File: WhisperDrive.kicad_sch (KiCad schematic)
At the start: 9 parts, among them J1 Fan+, J2 Fan+, J3 MOSFET-, J4 Fan-

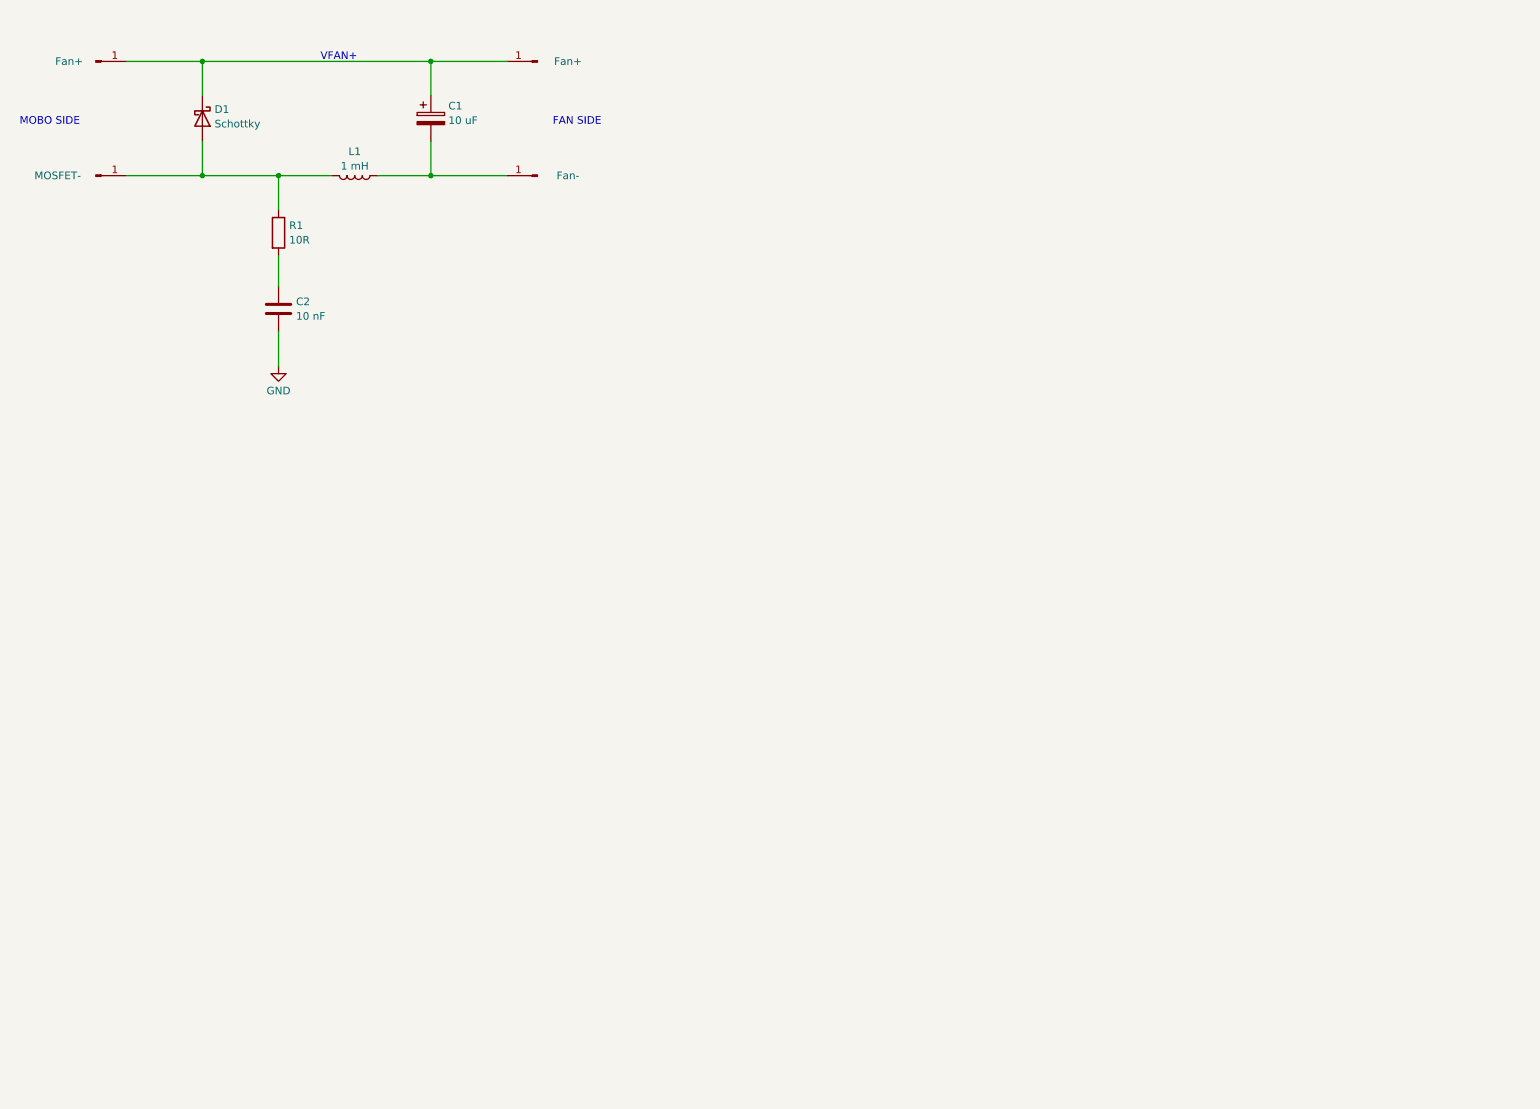
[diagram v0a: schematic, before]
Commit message: Further component selection and preliminary one-block layout for the switching only. Need buffer. Removed second block.
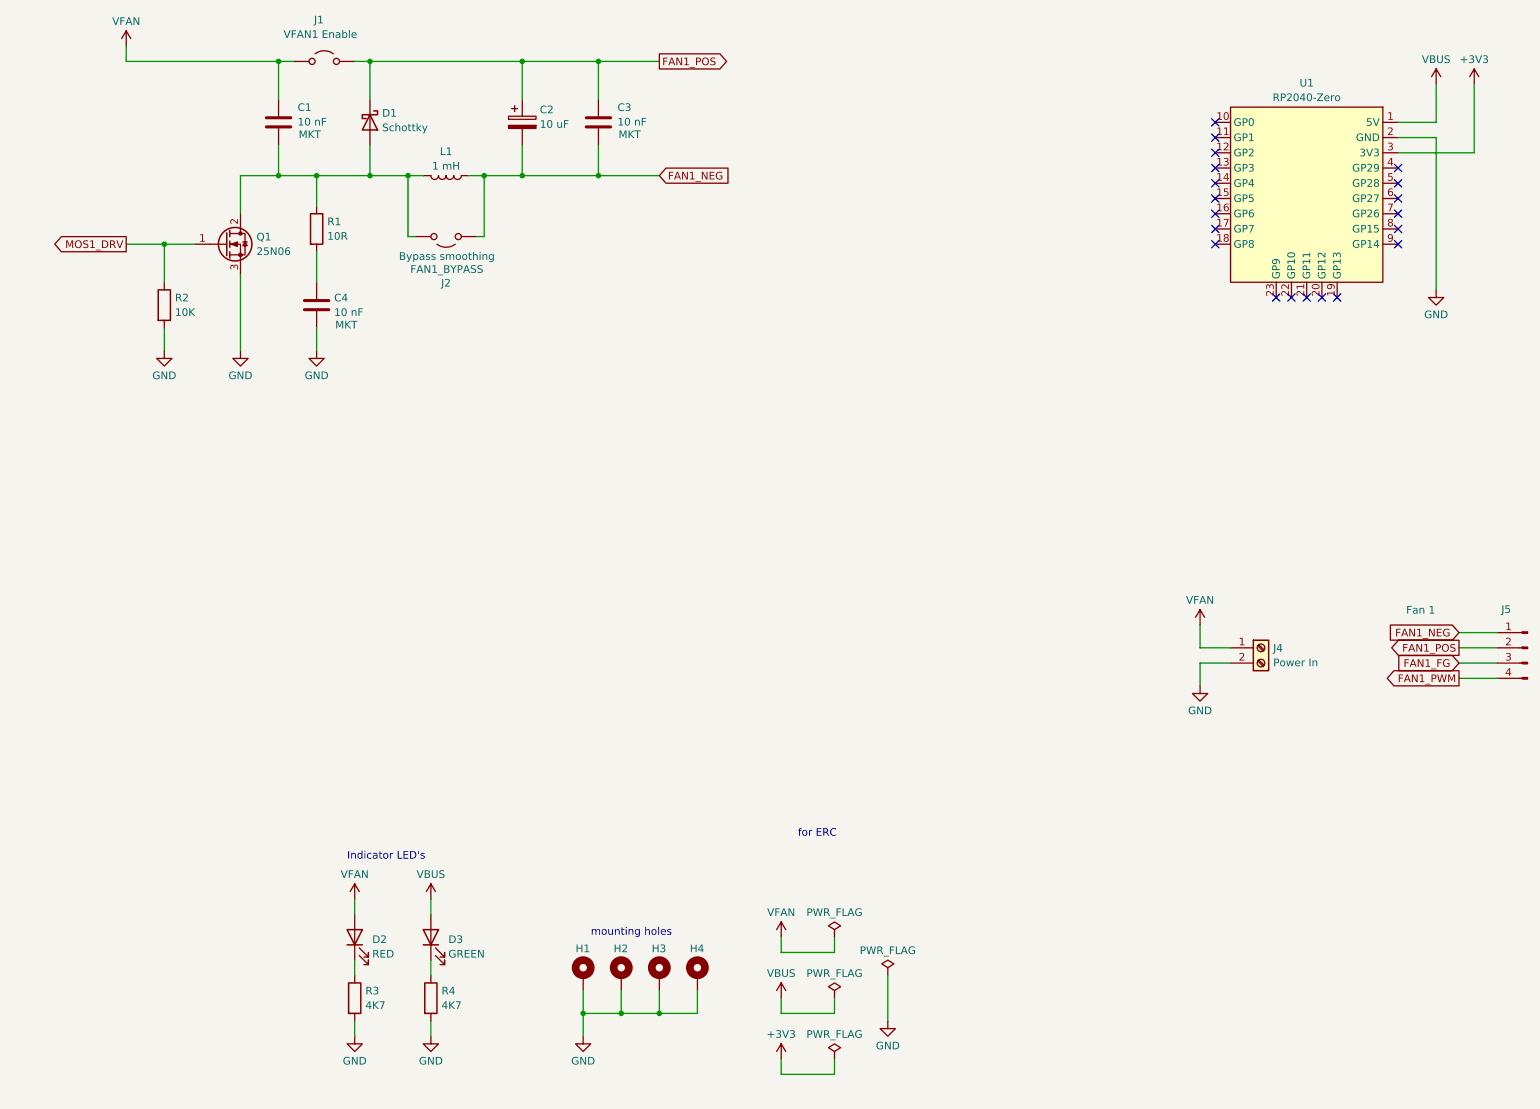
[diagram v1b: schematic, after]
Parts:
- removed J1, J2: Fan+, symbol Connector:Conn_01x01_Pin
- removed J3: MOSFET-, symbol Connector:Conn_01x01_Pin
- removed J4: Fan-, symbol Connector:Conn_01x01_Pin
- added C1, C3: 10 nF, Capacitor_THT:C_Disc_D6.0mm_W2.5mm_P5.00mm, symbol Device:C
- added D2: RED, LED_THT:LED_D3.0mm_Clear, symbol Device:LED
- added D3: GREEN, LED_THT:LED_D3.0mm_Clear, symbol Device:LED
- added H1, H2, H3, H4: MountingHole_Pad, MountingHole:MountingHole_3.2mm_M3, symbol Mechanical:MountingHole_Pad
- added J1: VFAN1 Enable, Jumper:SolderJumper-2_P1.3mm_Bridged2Bar_Pad1.0x1.5mm, symbol Jumper:Jumper_2_Open
- added J2: FAN1_BYPASS, Jumper:SolderJumper-2_P1.3mm_Open_Pad1.0x1.5mm, symbol Jumper:Jumper_2_Open
- added J4: Power In, symbol Connector:Screw_Terminal_01x02
- added J5: Fan 1, Connector_Molex:Molex_KK-254_AE-6410-04A_1x04_P2.54mm_Vertical, symbol Connector:Conn_01x04_Pin
- added Q1: 25N06, Package_TO_SOT_SMD:TO-252-3_TabPin2, symbol Transistor_FET:Q_NMOS_GDS
- added R2: 10K, Resistor_THT:R_Axial_DIN0204_L3.6mm_D1.6mm_P7.62mm_Horizontal, symbol Device:R
- added R3, R4: 4K7, Resistor_THT:R_Axial_DIN0204_L3.6mm_D1.6mm_P7.62mm_Horizontal, symbol Device:R
- added U1: RP2040-Zero, RP2040-Zero:RP2040 Zero, symbol RP2040-Zero:RP2040-Zero
- C2: renamed from C1; footprint (none) -> Capacitor_THT:CP_Radial_D5.0mm_P2.00mm
- C4: renamed from C2; footprint (none) -> Capacitor_THT:C_Disc_D6.0mm_W2.5mm_P5.00mm
- L1: footprint (none) -> Inductor_THT:L_Radial_D10.0mm_P5.00mm_Fastron_07M
- R1: footprint (none) -> Resistor_THT:R_Axial_DIN0204_L3.6mm_D1.6mm_P7.62mm_Horizontal
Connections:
- net GND: now also H1.1, H2.1, H3.1, H4.1, J4.2 (Pin_2), Q1.3 (S), R2.2, R3.2, R4.2, U1.2 (GND)
- net FAN1_POS: now reaches C2.1, D1.1 (K)
- net FAN1_POS: now also C3.1, J1.2 (B), J5.2 (Pin_2)
- net at D1.2 (A), L1.2, R1.1: now also C1.2, J2.2 (B), Q1.2 (D)
- net FAN1_NEG: now reaches C2.2, L1.1
- net FAN1_NEG: now also C3.2, J2.1 (A), J5.1 (Pin_1)
- new net: D2.1 (K), R3.1
- new net: D3.1 (K), R4.1
- new net +3V3: U1.3 (3V3)
- new net FAN1_FG: J5.3 (Pin_3)
- new net FAN1_PWM: J5.4 (Pin_4)
- new net MOS1_DRV: Q1.1 (G), R2.1
- new net VBUS: D3.2 (A), U1.1 (5V)
- new net VFAN: C1.1, D2.2 (A), J1.1 (A), J4.1 (Pin_1)
- no-connect marks 0 -> 20
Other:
- note added: "Indicator LED's"
- note added: "for ERC"
- note added: "mounting holes"
- note removed: "FAN SIDE"
- note removed: "MOBO SIDE"
- note removed: "VFAN+"
- moved on the sheet: C2, C4, D1, L1, R1

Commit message: DangerKlipper is Kalico now. + More changes not committed in the last commit. Oopsie.
Signed-off-by: HumbleDeer <djsndcx@gmail.com>
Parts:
- D1: footprint (none) -> Diode_THT:D_DO-41_SOD81_P10.16mm_Horizontal
- J4: footprint (none) -> TerminalBlock:TerminalBlock_MaiXu_MX126-5.0-02P_1x02_P5.00mm
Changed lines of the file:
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@@
 			)
 		)
-		(property "Footprint" ""
+		(property "Footprint" "Diode_THT:D_DO-41_SOD81_P10.16mm_Horizontal"
 			(at 78.74 35.56 0)
 			(effects
@@
 			)
 		)
-		(property "Footprint" ""
+		(property "Footprint" "TerminalBlock:TerminalBlock_MaiXu_MX126-5.0-02P_1x02_P5.00mm"
 			(at 227.33 123.19 0)
 			(effects

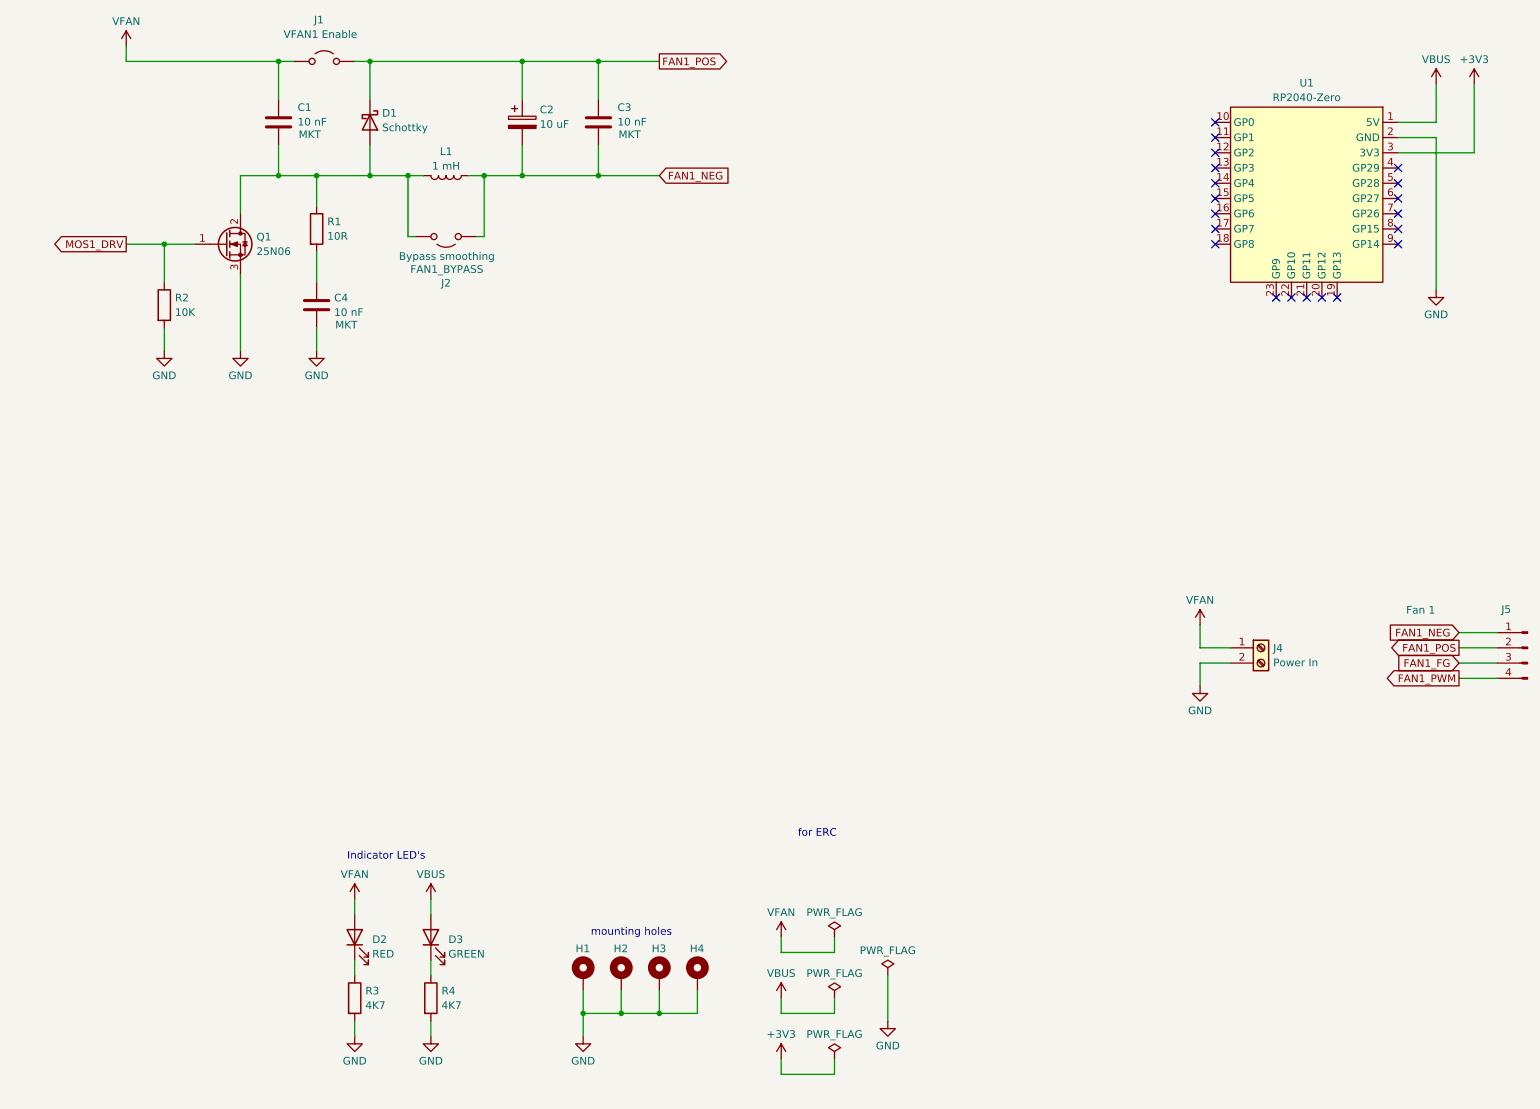
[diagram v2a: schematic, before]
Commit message: added: gate driver, second circuit, regulator for driver, optional separate power rail for fan/drive modified: changed global labels to net labels, moved power circuitry to subsheet
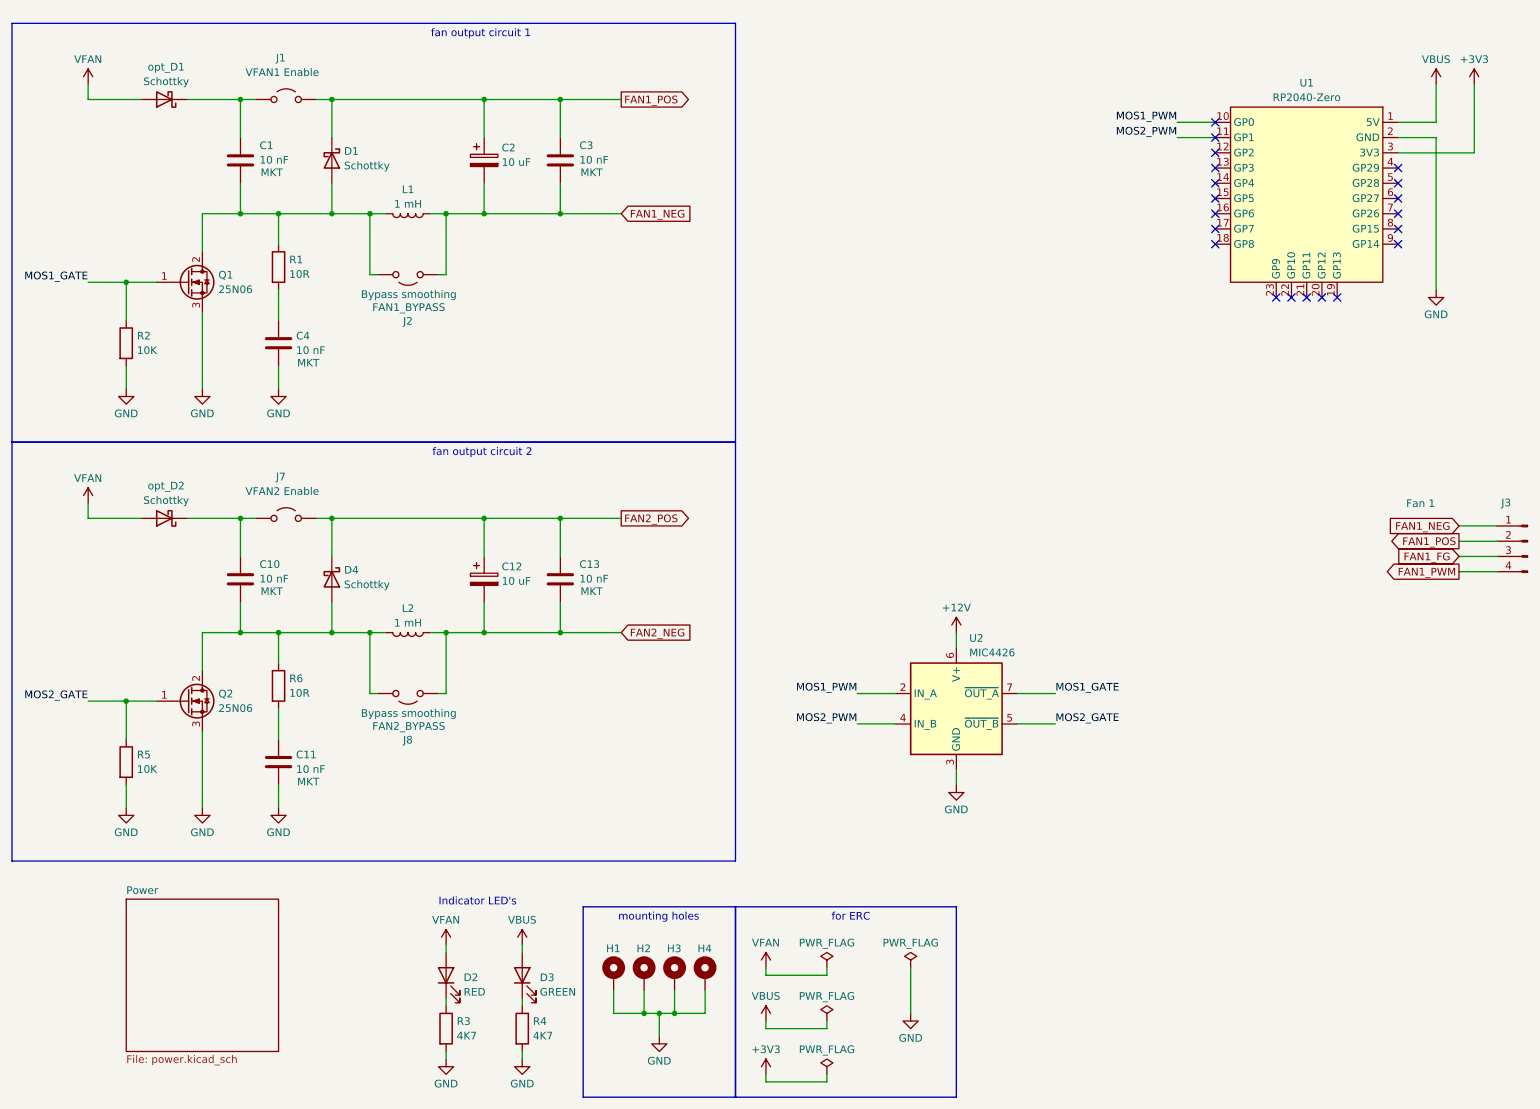
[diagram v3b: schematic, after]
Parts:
- removed J4: Power In, TerminalBlock:TerminalBlock_MaiXu_MX126-5.0-02P_1x02_P5.00mm, symbol Connector:Screw_Terminal_01x02
- added C10, C11, C13: 10 nF, Capacitor_THT:C_Disc_D6.0mm_W2.5mm_P5.00mm, symbol Device:C
- added C12: 10 uF, Capacitor_THT:CP_Radial_D5.0mm_P2.00mm, symbol Device:C_Polarized
- added D4, opt_D1, opt_D2: Schottky, Diode_THT:D_DO-41_SOD81_P10.16mm_Horizontal, symbol Device:D_Schottky
- added J7: VFAN2 Enable, Jumper:SolderJumper-2_P1.3mm_Bridged2Bar_Pad1.0x1.5mm, symbol Jumper:Jumper_2_Open
- added J8: FAN2_BYPASS, Jumper:SolderJumper-2_P1.3mm_Open_Pad1.0x1.5mm, symbol Jumper:Jumper_2_Open
- added L2: 1 mH, Inductor_THT:L_Radial_D10.0mm_P5.00mm_Fastron_07M, symbol Device:L
- added Q2: 25N06, Package_TO_SOT_SMD:TO-252-3_TabPin2, symbol Transistor_FET:Q_NMOS_GDS
- added R5: 10K, Resistor_THT:R_Axial_DIN0204_L3.6mm_D1.6mm_P7.62mm_Horizontal, symbol Device:R
- added R6: 10R, Resistor_THT:R_Axial_DIN0204_L3.6mm_D1.6mm_P7.62mm_Horizontal, symbol Device:R
- added U2: MIC4426, symbol Driver_FET:MIC4426
- renumbered J5 to J3
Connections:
- net GND: now also C11.2, Q2.3 (S), R5.2, U2.3 (GND)
- net VFAN: now also opt_D1.2 (A), opt_D2.2 (A); no longer C1.1, J1.1 (A)
- net MOS1_PWM: now reaches U1.10 (GP0)
- net MOS1_PWM: now also U2.2 (IN_A)
- net MOS2_PWM: now reaches U1.11 (GP1)
- net MOS2_PWM: now also U2.4 (IN_B)
- net MOS1_DRV renamed MOS1_GATE
- net MOS1_GATE: now also U2.7 (~{OUT_A})
- new net: C10.1, J7.1 (A), opt_D2.1 (K)
- new net: C10.2, D4.2 (A), J8.2 (B), L2.2, Q2.2 (D), R6.1
- new net: C1.1, J1.1 (A), opt_D1.1 (K)
- new net: C11.1, R6.2
- new net +12V: U2.6 (V+)
- new net FAN2_NEG: C12.2, C13.2, J8.1 (A), L2.1
- new net FAN2_POS: C12.1, C13.1, D4.1 (K), J7.2 (B)
- new net MOS2_GATE: Q2.1 (G), R5.1, U2.5 (~{OUT_B})
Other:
- added sheet Power (power.kicad_sch)
- note added: "fan output circuit 1"
- note added: "fan output circuit 2"
- moved on the sheet: C1, C2, C3, C4, D1, D2, D3, H1, H2, H3, H4, J1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
